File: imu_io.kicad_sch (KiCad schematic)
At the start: 6 parts, among them J1 USB_C_Receptacle_USB2.0_16P, J3 JST_PH2.0_01x04, J4 GPIO0, J5 GPIO1

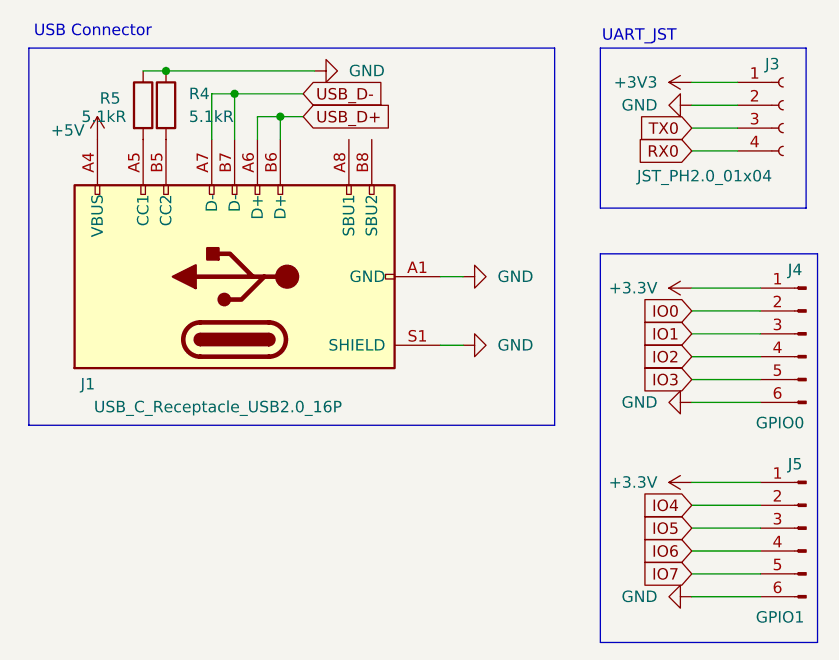
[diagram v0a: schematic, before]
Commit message: Route Traces for ESP32 and related IO
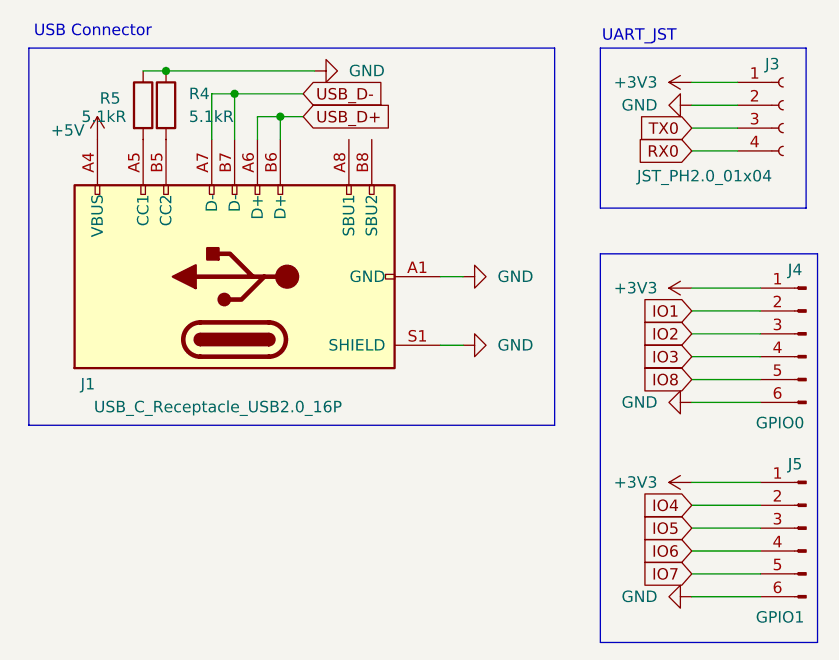
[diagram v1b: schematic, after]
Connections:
- net +3.3V is gone; now on net +3V3: J4.1 (Pin_1), J5.1 (Pin_1)
- net IO0 is gone; now on net IO1: J4.2 (Pin_2)
- net IO1: no longer J4.3 (Pin_3)
- net IO2: now also J4.3 (Pin_3); no longer J4.4 (Pin_4)
- net IO3: now also J4.4 (Pin_4); no longer J4.5 (Pin_5)
- new net IO8: J4.5 (Pin_5)
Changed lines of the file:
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@@
+	(wire
+		(pts
+			(xy 111.76 115.57) (xy 119.38 115.57)
+		)
+		(stroke
+			(width 0)
+			(type default)
+		)
+	)
+	(wire
+		(pts
+			(xy 111.76 73.66) (xy 116.84 73.66)
+		)
+		(stroke
+			(width 0)
+			(type default)
+		)
+	)
+	(wire
+		(pts
+			(xy 111.76 68.58) (xy 116.84 68.58)
+		)
+		(stroke
+			(width 0)
+			(type default)
+		)
+	)
+	(wire
+		(pts
+			(xy 58.42 69.85) (xy 60.96 69.85)
+		)
+		(stroke
+			(width 0)
+			(type default)
+		)
+	)
+	(wire
+		(pts
+			(xy 60.96 74.93) (xy 60.96 69.85)
+		)
+		(stroke
+			(width 0)
+			(type default)
+		)
+	)
+	(wire
+		(pts
+			(xy 111.76 113.03) (xy 119.38 113.03)
+		)
+		(stroke
+			(width 0)
+			(type default)
+		)
+	)
+	(wire
+		(pts
+			(xy 111.76 104.14) (xy 119.38 104.14)
+		)
+		(stroke
+			(width 0)
+			(type default)
+		)
+	)
+	(wire
+		(pts
+			(xy 111.76 91.44) (xy 119.38 91.44)
+		)
+		(stroke
+			(width 0)
+			(type default)
+		)
+	)
+	(wire
+		(pts
+			(xy 63.5 72.39) (xy 66.04 72.39)
+		)
+		(stroke
+			(width 0)
+			(type default)
+		)
+	)
+	(wire
+		(pts
+			(xy 83.82 90.17) (xy 86.36 90.17)
+		)
+		(stroke
+			(width 0)
+			(type default)
+		)
+	)
+	(wire
+		(pts
+			(xy 63.5 74.93) (xy 63.5 72.39)
+		)
+		(stroke
+			(width 0)
+			(type default)
+		)
+	)
+	(wire
+		(pts
+			(xy 60.96 69.85) (xy 68.58 69.85)
+		)
+		(stroke
+			(width 0)
+			(type default)
+		)
+	)
+	(wire
+		(pts
+			(xy 111.76 120.65) (xy 119.38 120.65)
+		)
+		(stroke
+			(width 0)
+			(type default)
+		)
+	)
+	(wire
+		(pts
+			(xy 66.04 72.39) (xy 68.58 72.39)
+		)
+		(stroke
+			(width 0)
+			(type default)
+		)
+	)
+	(wire
+		(pts
+			(xy 83.82 97.79) (xy 86.36 97.79)
+		)
+		(stroke
+			(width 0)
+			(type default)
+		)
+	)
+	(wire
+		(pts
+			(xy 111.76 99.06) (xy 119.38 99.06)
+		)
+		(stroke
+			(width 0)
+			(type default)
+		)
+	)
+	(wire
+		(pts
+			(xy 111.76 71.12) (xy 116.84 71.12)
+		)
+		(stroke
+			(width 0)
+			(type default)
+		)
+	)
 	(wire
 		(pts
@@
 	(wire
 		(pts
-			(xy 111.76 115.57) (xy 119.38 115.57)
-		)
-		(stroke
-			(width 0)
-			(type default)
-		)
-	)
-	(wire
-		(pts
-			(xy 111.76 73.66) (xy 116.84 73.66)
-		)
-		(stroke
-			(width 0)
-			(type default)
-		)
-	)
-	(wire
-		(pts
-			(xy 111.76 68.58) (xy 116.84 68.58)
-		)
-		(stroke
-			(width 0)
-			(type default)
-		)
-	)
-	(wire
-		(pts
-			(xy 58.42 69.85) (xy 60.96 69.85)
-		)
-		(stroke
-			(width 0)
-			(type default)
-		)
-	)
-	(wire
-		(pts
-			(xy 60.96 74.93) (xy 60.96 69.85)
-		)
-		(stroke
-			(width 0)
-			(type default)
-		)
-	)
-	(wire
-		(pts
-			(xy 111.76 99.06) (xy 119.38 99.06)
-		)
-		(stroke
-			(width 0)
-			(type default)
-		)
-	)
-	(wire
-		(pts
-			(xy 111.76 113.03) (xy 119.38 113.03)
-		)
-		(stroke
-			(width 0)
-			(type default)
-		)
-	)
-	(wire
-		(pts
-			(xy 111.76 104.14) (xy 119.38 104.14)
-		)
-		(stroke
-			(width 0)
-			(type default)
-		)
-	)
-	(wire
-		(pts
-			(xy 111.76 91.44) (xy 119.38 91.44)
-		)
-		(stroke
-			(width 0)
-			(type default)
-		)
-	)
-	(wire
-		(pts
-			(xy 63.5 72.39) (xy 66.04 72.39)
-		)
-		(stroke
-			(width 0)
-			(type default)
-		)
-	)
-	(wire
-		(pts
-			(xy 83.82 90.17) (xy 86.36 90.17)
-		)
-		(stroke
-			(width 0)
-			(type default)
-		)
-	)
-	(wire
-		(pts
-			(xy 63.5 74.93) (xy 63.5 72.39)
-		)
-		(stroke
-			(width 0)
-			(type default)
-		)
-	)
-	(wire
-		(pts
-			(xy 60.96 69.85) (xy 68.58 69.85)
-		)
-		(stroke
-			(width 0)
-			(type default)
-		)
-	)
-	(wire
-		(pts
-			(xy 111.76 120.65) (xy 119.38 120.65)
-		)
-		(stroke
-			(width 0)
-			(type default)
-		)
-	)
-	(wire
-		(pts
-			(xy 66.04 72.39) (xy 68.58 72.39)
-		)
-		(stroke
-			(width 0)
-			(type default)
-		)
-	)
-	(wire
-		(pts
-			(xy 83.82 97.79) (xy 86.36 97.79)
-		)
-		(stroke
-			(width 0)
-			(type default)
-		)
-	)
-	(wire
-		(pts
-			(xy 111.76 71.12) (xy 116.84 71.12)
-		)
-		(stroke
-			(width 0)
-			(type default)
-		)
-	)
-	(wire
-		(pts
 			(xy 111.76 118.11) (xy 119.38 118.11)
 		)
@@
 	(wire
 		(pts
+			(xy 58.42 74.93) (xy 58.42 69.85)
+		)
+		(stroke
+			(width 0)
+			(type default)
+		)
+	)
+	(wire
+		(pts
 			(xy 111.76 96.52) (xy 119.38 96.52)
-		)
-		(stroke
-			(width 0)
-			(type default)
-		)
-	)
-	(wire
-		(pts
-			(xy 58.42 74.93) (xy 58.42 69.85)
 		)
 		(stroke
@@
 	(global_label "IO2"
 		(shape input)
-		(at 111.76 99.06 180)
+		(at 111.76 96.52 180)
 		(fields_autoplaced yes)
 		(effects
@@
 		)
 		(property "Intersheetrefs" "${INTERSHEET_REFS}"
-			(at 105.63 99.06 0)
+			(at 105.63 96.52 0)
 			(effects
 				(font
@@
 	(global_label "IO3"
 		(shape input)
-		(at 111.76 101.6 180)
+		(at 111.76 99.06 180)
 		(fields_autoplaced yes)
 		(effects
@@
 		)
 		(property "Intersheetrefs" "${INTERSHEET_REFS}"
-			(at 105.63 101.6 0)
+			(at 105.63 99.06 0)
 			(effects
 				(font
@@
 		)
 	)
-	(global_label "IO0"
+	(global_label "IO1"
 		(shape input)
 		(at 111.76 93.98 180)
@@
 		)
 	)
-	(global_label "IO1"
+	(global_label "IO7"
 		(shape input)
-		(at 111.76 96.52 180)
+		(at 111.76 123.19 180)
 		(fields_autoplaced yes)
 		(effects
@@
 		)
 		(property "Intersheetrefs" "${INTERSHEET_REFS}"
-			(at 105.63 96.52 0)
-			(effects
-				(font
-					(size 1.27 1.27)
-				)
-				(justify right)
-				(hide yes)
-			)
-		)
-	)
-	(global_label "IO7"
+			(at 105.63 123.19 0)
+			(effects
+				(font
+					(size 1.27 1.27)
+				)
+				(justify right)
+				(hide yes)
+			)
+		)
+	)
+	(global_label "IO4"
 		(shape input)
-		(at 111.76 123.19 180)
+		(at 111.76 115.57 180)
 		(fields_autoplaced yes)
 		(effects
@@
 		)
 		(property "Intersheetrefs" "${INTERSHEET_REFS}"
-			(at 105.63 123.19 0)
-			(effects
-				(font
-					(size 1.27 1.27)
-				)
-				(justify right)
-				(hide yes)
-			)
-		)
-	)
-	(global_label "IO4"
+			(at 105.63 115.57 0)
+			(effects
+				(font
+					(size 1.27 1.27)
+				)
+				(justify right)
+				(hide yes)
+			)
+		)
+	)
+	(global_label "IO8"
 		(shape input)
-		(at 111.76 115.57 180)
+		(at 111.76 101.6 180)
 		(fields_autoplaced yes)
 		(effects
@@
 		)
 		(property "Intersheetrefs" "${INTERSHEET_REFS}"
-			(at 105.63 115.57 0)
+			(at 105.63 101.6 0)
 			(effects
 				(font
@@
 			)
 		)
-		(property "Value" "+3.3V"
+		(property "Value" "+3V3"
 			(at 107.95 113.0299 90)
 			(effects
@@
 			)
 		)
-		(property "Value" "+3.3V"
+		(property "Value" "+3V3"
 			(at 107.95 91.4399 90)
 			(effects

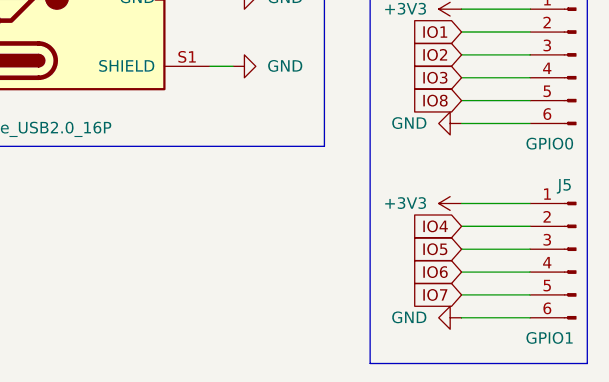
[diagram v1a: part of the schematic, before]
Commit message: Add Sensors and Silkscreen Adjustments
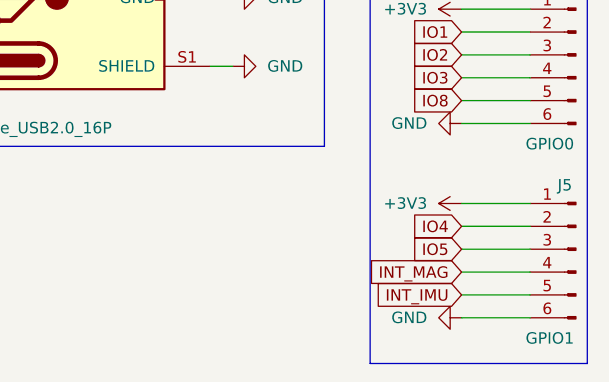
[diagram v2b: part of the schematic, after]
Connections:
- net IO6 renamed INT_MAG
- net IO7 renamed INT_IMU
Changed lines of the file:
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@@
+		)
+	)
+	(global_label "INT_IMU"
+		(shape input)
+		(at 111.76 123.19 180)
+		(fields_autoplaced yes)
+		(effects
+			(font
+				(size 1.27 1.27)
+			)
+			(justify right)
+		)
+		(property "Intersheetrefs" "${INTERSHEET_REFS}"
+			(at 101.5176 123.19 0)
+			(effects
+				(font
+					(size 1.27 1.27)
+				)
+				(justify right)
+				(hide yes)
+			)
 		)
 	)
@@
 		)
 	)
-	(global_label "IO6"
-		(shape input)
-		(at 111.76 120.65 180)
-		(fields_autoplaced yes)
-		(effects
-			(font
-				(size 1.27 1.27)
-			)
-			(justify right)
-		)
-		(property "Intersheetrefs" "${INTERSHEET_REFS}"
-			(at 105.63 120.65 0)
-			(effects
-				(font
-					(size 1.27 1.27)
-				)
-				(justify right)
-				(hide yes)
-			)
-		)
-	)
 	(global_label "IO1"
 		(shape input)
@@
 		)
 	)
-	(global_label "IO7"
+	(global_label "INT_MAG"
 		(shape input)
-		(at 111.76 123.19 180)
+		(at 111.76 120.65 180)
 		(fields_autoplaced yes)
 		(effects
@@
 		)
 		(property "Intersheetrefs" "${INTERSHEET_REFS}"
-			(at 105.63 123.19 0)
+			(at 101.0943 120.65 0)
 			(effects
 				(font
